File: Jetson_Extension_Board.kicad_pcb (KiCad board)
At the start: 2 copper layers, 90 x 77 mm, 28 parts, among them J1 I2C_2 DEBUG, J10 TBP03R2-350-03BE, J11 ST DEBUG, J12 TBP03R2-350-03BE, J13 TBP03R2-350-03BE, J14 IMU_6, J15 IMU_4, J19 external i2c bus, J2 TBP03R2-350-03BE, J3 TBP03R2-350-03BE, J4 TBP03R2-350-03BE, J5 TBP03R2-350-03BE, J6 40_Pin_Jetson_Connector, J7 TBP03R2-350-03BE, J8 TBP03R2-350-03BE, J9 TBP03R2-350-03BE, SW1 SW_Push_DPDT, U2 74LV14, U4 ADS1115IDGS

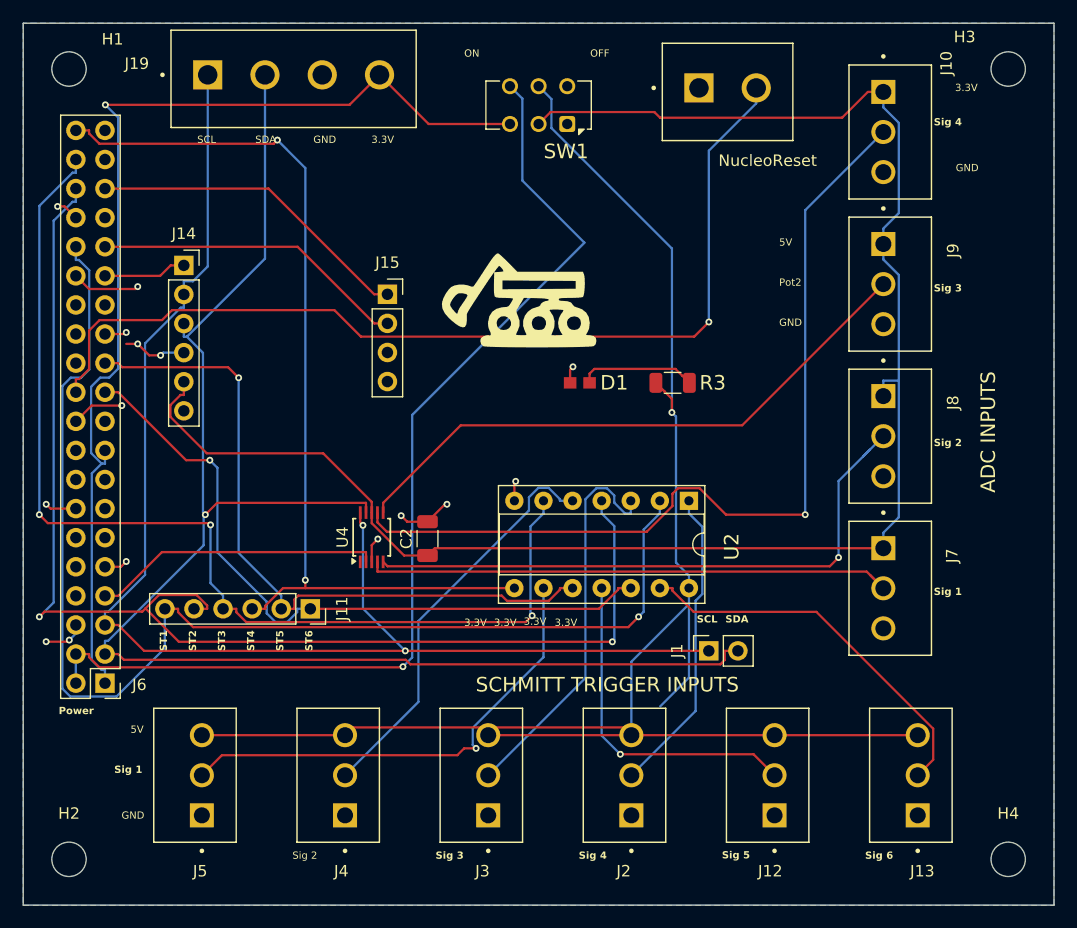
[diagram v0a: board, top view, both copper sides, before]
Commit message: labels moved
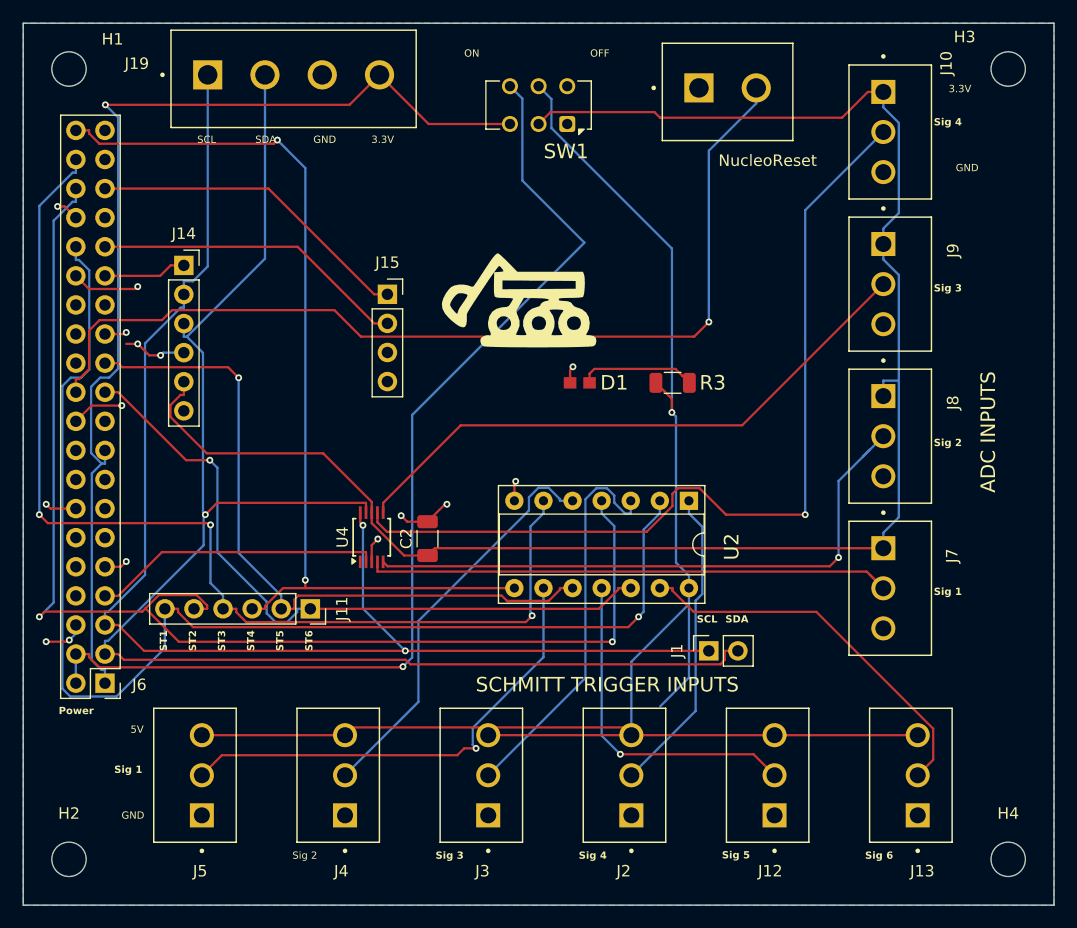
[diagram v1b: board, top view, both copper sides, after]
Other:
- board text removed: "Pot2"
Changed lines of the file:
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@@
-		)
-	)
-	(gr_text "3.3V"
-		(at 131.4 123.7 0)
-		(layer "F.SilkS")
-		(effects
-			(font
-				(size 0.635 0.635)
-				(thickness 0.127)
-			)
-			(justify left bottom)
 		)
 	)
@@
 		)
 	)
-	(gr_text "3.3V"
-		(at 123.5 123.7 0)
-		(layer "F.SilkS")
-		(effects
-			(font
-				(size 0.635 0.635)
-				(thickness 0.127)
-			)
-			(justify left bottom)
-		)
-	)
 	(gr_text "Sig 2"
 		(at 164.5 108 0)
@@
 		)
 	)
-	(gr_text "GND"
-		(at 151 97.5 0)
-		(layer "F.SilkS")
-		(effects
-			(font
-				(size 0.635 0.635)
-				(thickness 0.127)
-			)
-			(justify left bottom)
-		)
-	)
 	(gr_text "ST5"
 		(at 107.79 125.83 90)
@@
 		)
 	)
-	(gr_text "Pot2"
-		(at 151 94 0)
-		(layer "F.SilkS")
-		(effects
-			(font
-				(size 0.635 0.635)
-				(thickness 0.127)
-			)
-			(justify left bottom)
-		)
-	)
 	(gr_text "Sig 5"
 		(at 146 144 0)
@@
 	)
 	(gr_text "3.3V"
-		(at 166.357024 77 0)
+		(at 165.8 77.1 0)
 		(layer "F.SilkS")
 		(effects
@@
 		)
 	)
-	(gr_text "5V\n"
-		(at 151 90.5 0)
-		(layer "F.SilkS")
-		(effects
-			(font
-				(size 0.635 0.635)
-				(thickness 0.127)
-			)
-			(justify left bottom)
-		)
-	)
 	(gr_text "GND"
 		(at 93.582501 140.5325 0)
@@
 		(layer "F.SilkS")
 		(effects
-			(font
-				(size 0.635 0.635)
-				(thickness 0.127)
-			)
-			(justify left bottom)
-		)
-	)
-	(gr_text "3.3V"
-		(at 126.1 123.7 0)
-		(layer "F.SilkS")
-		(effects
-			(font
-				(size 0.635 0.635)
-				(thickness 0.127)
-			)
-			(justify left bottom)
-		)
-	)
-	(gr_text "3.3V"
-		(at 128.7 123.6 0)
-		(layer "F.SilkS")
-		(effects

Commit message: Modified constraints and routing
Set constraints according to JLCPCB specifications.
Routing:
- net /SchmittTrigger(74LV14)/5V: track 153.0 -> 131.8 mm
- net GND: track 38.8 -> 23.4 mm, vias 15 -> 10
- net 3.3V: track 93.4 -> 107.9 mm, vias 1 -> 0
- net 5V: track 91.7 -> 94.3 mm
- net /ADC/Signal 1: track 46.1 -> 48.5 mm
- net ST 2: track 110.9 -> 109.7 mm
- net SCL: track 119.9 -> 121.1 mm
- net /ADC/3.3V: track 148.8 -> 147.9 mm
- net /ADC/Signal 2: track 53.3 -> 52.4 mm
- net ST 5: track 61.0 -> 60.5 mm
- net /ADC/Signal 4: track 77.9 -> 78.5 mm

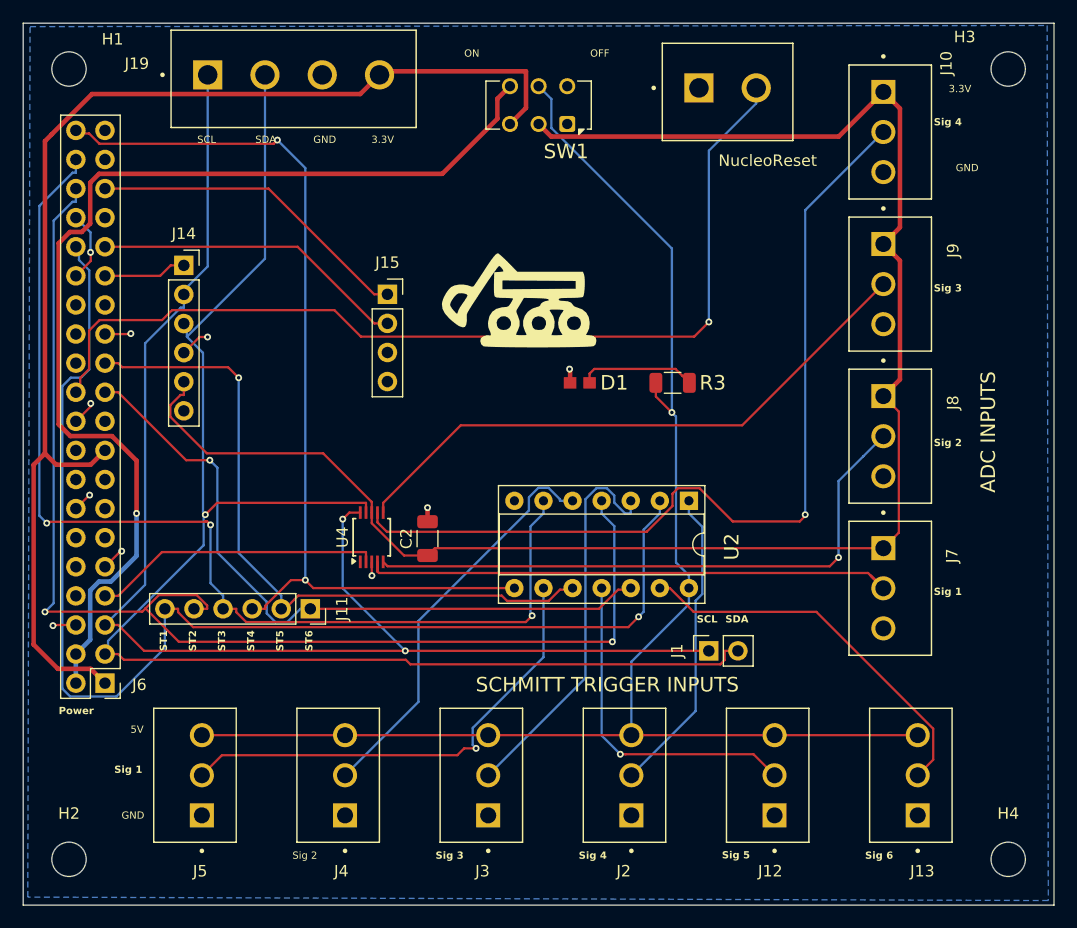
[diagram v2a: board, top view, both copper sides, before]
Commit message: Generated Gerbers
Also made slight modifications to routing and added board info to back silkscreen
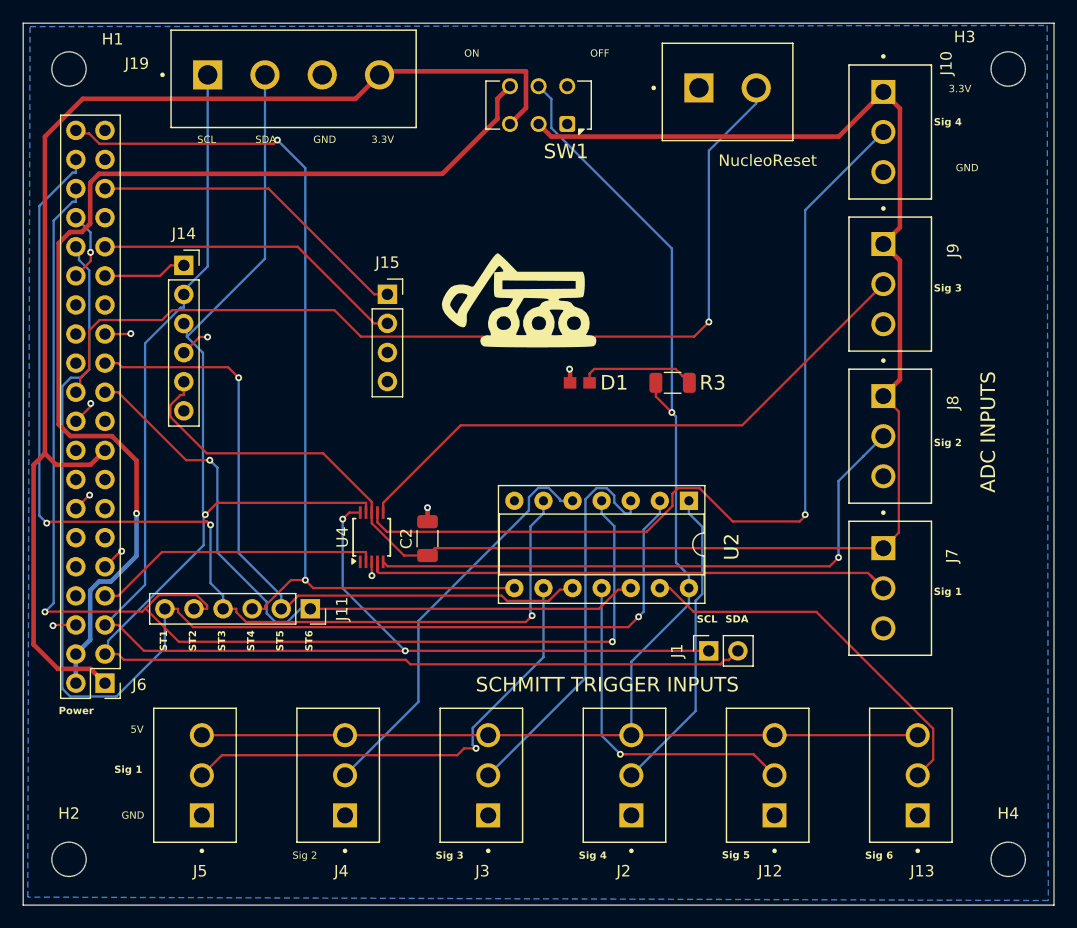
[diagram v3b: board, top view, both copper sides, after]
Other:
- board text added: "Jetson Extension Board 2/27/2025 Rev. 3"
- board text removed: "Jetson Extension Board 2/2/2025 Rev. 2"
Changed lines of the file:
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@@
 			(drillshape 0)
 			(scaleselection 1)
-			(outputdirectory "../../Downloads/")
+			(outputdirectory "Gerber and Drill Files/JEB_rev3_gerber/")
 		)
 	)
@@
 		(layer "Edge.Cuts")
 	)
-	(gr_text "Jetson Extension Board\n2/2/2025 Rev. 2"
-		(at 112.9 89.5 0)
-		(layer "F.Paste")
+	(gr_text "Jetson Extension Board\n2/27/2025 Rev. 3"
+		(at 112.7 90.6 0)
+		(layer "B.SilkS")
 		(effects
 			(font
@@
 				(thickness 0.3)
 			)
-			(justify left bottom)
+			(justify right bottom mirror)
 		)
 	)
@@
 	)
 	(segment
-		(start 87.5 80.7)
-		(end 86.9 81.3)
-		(width 0.4)
-		(layer "F.Cu")
-		(net 2)
-	)
-	(segment
 		(start 90.89 127.37)
 		(end 88.03 127.37)
@@
 	)
 	(segment
-		(start 92.14 128.62)
-		(end 90.89 127.37)
+		(start 116.11 75.51)
+		(end 114.02 77.6)
 		(width 0.4)
 		(layer "F.Cu")
@@
 	)
 	(segment
-		(start 116.11 75.51)
-		(end 116.42 75.2)
+		(start 86.9 80.9)
+		(end 86.9 108.567766)
 		(width 0.4)
 		(layer "F.Cu")
@@
 	)
 	(segment
-		(start 86.9 108.567766)
-		(end 87.882234 109.55)
+		(start 92.14 128.62)
+		(end 90.89 127.37)
 		(width 0.4)
 		(layer "F.Cu")
@@
 	)
 	(segment
-		(start 85.909695 125.249695)
-		(end 85.909695 109.558072)
+		(start 90.2 77.6)
+		(end 86.9 80.9)
 		(width 0.4)
 		(layer "F.Cu")
@@
 	)
 	(segment
-		(start 114.435 77.185)
-		(end 91.007233 77.185)
+		(start 116.11 75.51)
+		(end 116.42 75.2)
 		(width 0.4)
 		(layer "F.Cu")
@@
 	)
 	(segment
-		(start 116.42 75.2)
-		(end 128.9 75.2)
+		(start 86.9 108.567766)
+		(end 87.882234 109.55)
 		(width 0.4)
 		(layer "F.Cu")
@@
 	)
 	(segment
-		(start 87.5 80.692233)
-		(end 87.5 80.7)
+		(start 85.909695 125.249695)
+		(end 85.909695 109.558072)
 		(width 0.4)
 		(layer "F.Cu")
@@
 	)
 	(segment
-		(start 91.007233 77.185)
-		(end 87.5 80.692233)
+		(start 116.42 75.2)
+		(end 128.9 75.2)
 		(width 0.4)
 		(layer "F.Cu")
@@
 	)
 	(segment
-		(start 86.9 81.3)
-		(end 86.9 108.567766)
+		(start 90.89 109.55)
+		(end 92.14 108.3)
 		(width 0.4)
 		(layer "F.Cu")
@@
 	)
 	(segment
-		(start 116.11 75.51)
-		(end 114.435 77.185)
+		(start 87.882234 109.55)
+		(end 90.89 109.55)
 		(width 0.4)
 		(layer "F.Cu")
@@
 	)
 	(segment
-		(start 90.89 109.55)
-		(end 92.14 108.3)
-		(width 0.4)
-		(layer "F.Cu")
-		(net 2)
-	)
-	(segment
-		(start 87.882234 109.55)
-		(end 90.89 109.55)
+		(start 114.02 77.6)
+		(end 90.2 77.6)
 		(width 0.4)
 		(layer "F.Cu")
@@
 	)
 	(segment
-		(start 147.4 125.8)
-		(end 146.248 125.8)
-		(width 0.2)
-		(layer "F.Cu")
-		(net 17)
-	)
-	(segment
 		(start 145.864 126.976)
 		(end 118.802 126.976)
@@
 	)
 	(segment
+		(start 146.248 126.592)
+		(end 146.608 126.592)
+		(width 0.2)
+		(layer "F.Cu")
+		(net 17)
+	)
+	(segment
 		(start 93.2917 126.08)
 		(end 92.14 126.08)
@@
 	)
 	(segment
-		(start 146.248 125.8)
-		(end 146.248 126.592)
+		(start 146.608 126.592)
+		(end 147.4 125.8)
 		(width 0.2)
 		(layer "F.Cu")

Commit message: v4 pcb
drc: didn't connect 3.3v pins and 5v pins and some gnd pins are not connected to gnd plane; they are connected within the jetson, and I don't think it's necessary to connect them on the jeb. all components are connected  to corresponding pins
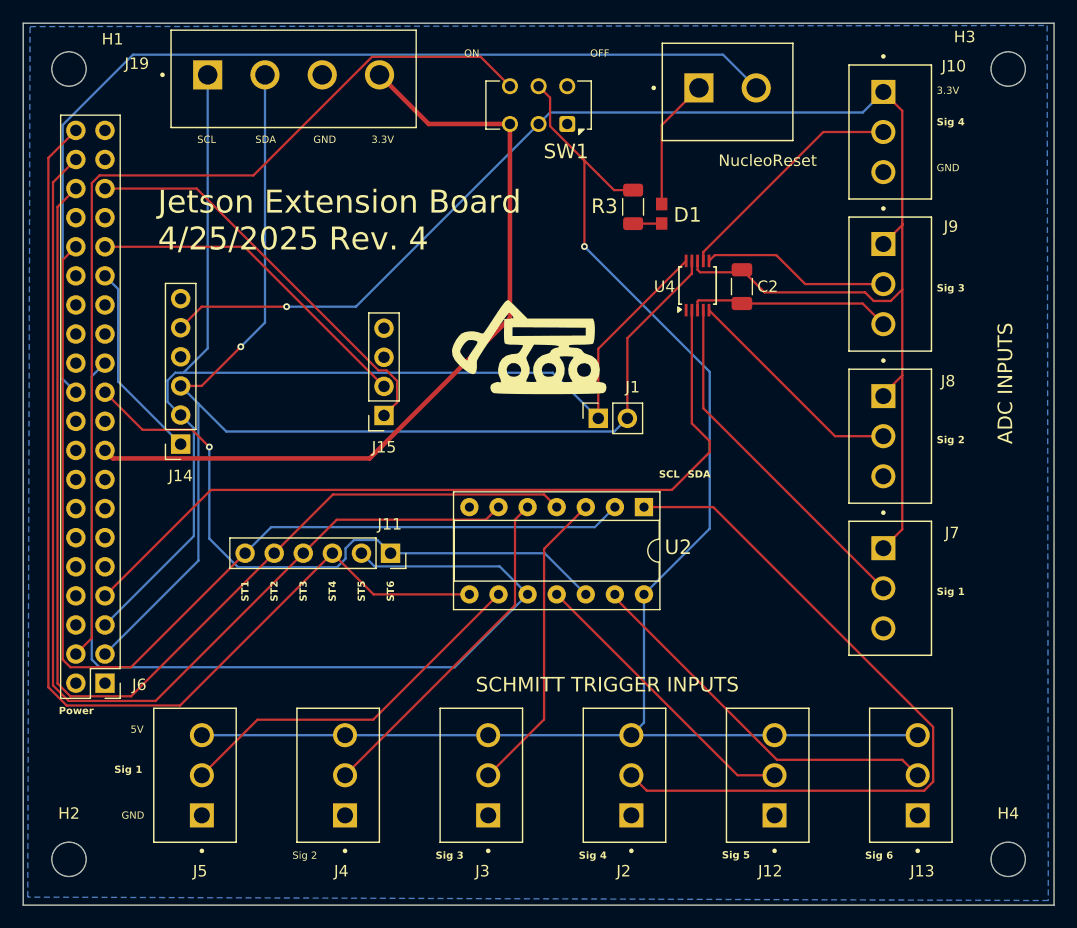
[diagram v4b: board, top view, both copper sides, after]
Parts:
- moved U4 35.9 mm to (143.9, 93.9)
- moved C2 35.2 mm to (147.8, 94.0), turned to -90 degrees
- moved J1 22.5 mm to (135.2, 105.5)
- moved D1 16.4 mm to (140.8, 87.6), turned to -90 degrees
- moved R3 15.7 mm to (138.2, 87.0), turned to -90 degrees
- moved J14 15.6 mm to (98.8, 107.8), turned to 180 degrees
- moved J15 10.6 mm to (116.5, 105.2), turned to 180 degrees
- moved J11 8.52 mm to (117.1, 117.3)
- moved G*** 4.18 mm to (129.5, 99.8)
- moved U2 3.96 mm to (139.2, 113.2)
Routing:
- net /ADC/Signal 4: track 78.5 -> 20.8 mm, vias 1 -> 0
- net ADC ALERT: track 25.2 -> 71.0 mm
- net Net-(J2-Pad2): track 27.0 -> 65.2 mm
- net 3.3V: track 108.1 -> 70.8 mm
- net /ADC/Signal 3: track 52.4 -> 16.5 mm
- net /ADC/Signal 2: track 52.4 -> 19.8 mm, vias 1 -> 0
- net ST 5: track 60.5 -> 83.3 mm, vias 1 -> 0
- net /ADC/Signal 1: track 48.5 -> 30.8 mm
- net ST 1: track 108.4 -> 90.8 mm, vias 1 -> 0
- net SDA: track 130.4 -> 113.7 mm
- net ST 2: track 109.7 -> 95.7 mm, vias 2 -> 0
- net SCL: track 121.1 -> 108.9 mm, vias 2 -> 0
- net ST 4: track 82.0 -> 94.0 mm, vias 2 -> 0
- net /ADC/3.3V: track 147.9 -> 136.4 mm, vias 0 -> 1
- net 5V: track 94.3 -> 83.8 mm, vias 1 -> 0
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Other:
- board text added: "Jetson Extension Board 4/25/2025 Rev. 4"
- board text removed: "Jetson Extension Board 2/27/2025 Rev. 3"

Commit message: updates
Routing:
- net GND: track 29.4 -> 39.6 mm
- net ST 5: track 83.3 -> 89.0 mm
- net /gpio13: track 88.1 -> 89.3 mm
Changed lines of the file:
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@@
+	)
+	(segment
+		(start 116.5 100.17)
+		(end 116.5 97.63)
+		(width 0.2)
+		(layer "F.Cu")
+		(net 1)
+	)
+	(segment
+		(start 98.75 100.13)
+		(end 94.13 100.13)
+		(width 0.2)
+		(layer "F.Cu")
+		(net 1)
+	)
+	(segment
+		(start 94.13 100.13)
+		(end 92.14 98.14)
+		(width 0.2)
+		(layer "F.Cu")
+		(net 1)
+	)
+	(segment
+		(start 132.65 76.65)
+		(end 132.5 76.5)
+		(width 0.2)
+		(layer "F.Cu")
+		(net 1)
 	)
 	(segment
@@
 	)
 	(segment
-		(start 93.29 102.29)
-		(end 93.29 94.21)
+		(start 94.75 95.67)
+		(end 92.14 93.06)
 		(width 0.2)
 		(layer "B.Cu")
@@
 	)
 	(segment
+		(start 94.75 103.75)
+		(end 94.75 95.67)
+		(width 0.2)
+		(layer "B.Cu")
+		(net 15)
+	)
+	(segment
 		(start 98.75 107.75)
-		(end 93.29 102.29)
-		(width 0.2)
-		(layer "B.Cu")
-		(net 15)
-	)
-	(segment
-		(start 93.29 94.21)
-		(end 92.14 93.06)
+		(end 94.75 103.75)
 		(width 0.2)
 		(layer "B.Cu")
@@
 	)
 	(segment
-		(start 88.45 79.883654)
+		(start 87 81.333654)
 		(end 94.583654 73.75)
 		(width 0.2)
@@
 	)
 	(segment
+		(start 87 100.62)
+		(end 87 81.333654)
+		(width 0.2)
+		(layer "B.Cu")
+		(net 31)
+	)
+	(segment
 		(start 146.1 73.75)
 		(end 149 76.65)
@@
 	(segment
 		(start 89.6 103.22)
-		(end 88.45 102.07)
-		(width 0.2)
-		(layer "B.Cu")
-		(net 31)
-	)
-	(segment
-		(start 88.45 102.07)
-		(end 88.45 79.883654)
+		(end 87 100.62)
 		(width 0.2)
 		(layer "B.Cu")
@@
 	)
 	(segment
-		(start 129.04 120.87)
-		(end 122.68 127.23)
-		(width 0.2)
-		(layer "B.Cu")
-		(net 43)
-	)
-	(segment
 		(start 126.595 118.425)
 		(end 115.685 118.425)
@@
 	)
 	(segment
-		(start 91.663654 127.23)
-		(end 90.99 126.556346)
+		(start 87.5 104.75)
+		(end 87.5 125.606346)
 		(width 0.2)
 		(layer "B.Cu")
@@
 	)
 	(segment
-		(start 90.99 101.83)
-		(end 92.14 100.68)
+		(start 90.75 103.696346)
+		(end 90.076346 104.37)
 		(width 0.2)
 		(layer "B.Cu")
@@
 	)
 	(segment
-		(start 90.99 126.556346)
-		(end 90.99 101.83)
+		(start 89.123654 127.23)
+		(end 122.68 127.23)
 		(width 0.2)
 		(layer "B.Cu")
@@
 	)
 	(segment
-		(start 122.68 127.23)
-		(end 91.663654 127.23)
+		(start 92.14 100.68)
+		(end 90.75 102.07)
+		(width 0.2)
+		(layer "B.Cu")
+		(net 43)
+	)
+	(segment
+		(start 90.75 102.07)
+		(end 90.75 103.696346)
 		(width 0.2)
 		(layer "B.Cu")
@@
 	)
 	(segment
+		(start 122.68 127.23)
+		(end 129.04 120.87)
+		(width 0.2)
+		(layer "B.Cu")
+		(net 43)
+	)
+	(segment
 		(start 129.04 120.87)
 		(end 126.595 118.425)
 		(width 0.2)
 		(layer "B.Cu")
+		(net 43)
+	)
+	(segment
+		(start 87.88 104.37)
+		(end 87.5 104.75)
+		(width 0.2)
+		(layer "B.Cu")
+		(net 43)
+	)
+	(segment
+		(start 90.076346 104.37)
+		(end 87.88 104.37)
+		(width 0.2)
+		(layer "B.Cu")
+		(net 43)
+	)
+	(segment
+		(start 87.5 125.606346)
+		(end 89.123654 127.23)
+		(width 0.2)
+		(layer "B.Cu")
